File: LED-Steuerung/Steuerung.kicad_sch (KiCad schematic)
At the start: 45 parts, among them J1 DNP, J10 Barrel_Jack_Switch, J2 Conn_02x03_Odd_Even, J3 DNP, J4 Conn_01x01_Female, J5 Conn_01x01_Female, J6 Conn_01x01_Female, J7 Conn_01x01_Female, J8 Conn_01x01_Female, J9 Conn_01x01_Female, SW1 SW_Push, U1 STM32WB5MMG, U2 L7983, U3 INA186A3IDDF

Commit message: wip
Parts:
- added R11: 10k, Resistor_SMD:R_0603_1608Metric, symbol Device:R
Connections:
- net GND: now also R11.1; no longer U1.32 (VDDUSB)
- new net: R11.2, U1.32 (VDDUSB)
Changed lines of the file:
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@@
-    (stroke (width 0) (type default) (color 0 0 0 0))
-  )
-  (wire (pts (xy 71.12 66.04) (xy 71.12 68.58))
     (stroke (width 0) (type default) (color 0 0 0 0))
   )
@@
     (pin "1")
   )
-  (symbol (lib_id "power:GND") (at 71.12 66.04 180) (unit 1)
-    (in_bom yes) (on_board yes)
-    (property "Reference" "#PWR013" (id 0) (at 71.12 59.69 0)
-      (effects (font (size 1.27 1.27)) hide)
-    )
-    (property "Value" "GND" (id 1) (at 71.12 62.23 90)
-      (effects (font (size 1.27 1.27)) (justify right))
-    )
-    (property "Footprint" "" (id 2) (at 71.12 66.04 0)
-      (effects (font (size 1.27 1.27)) hide)
-    )
-    (property "Datasheet" "" (id 3) (at 71.12 66.04 0)
+  (symbol (lib_id "power:GND") (at 71.12 60.96 180) (unit 1)
+    (in_bom yes) (on_board yes)
+    (property "Reference" "#PWR013" (id 0) (at 71.12 54.61 0)
+      (effects (font (size 1.27 1.27)) hide)
+    )
+    (property "Value" "GND" (id 1) (at 71.12 57.15 90)
+      (effects (font (size 1.27 1.27)) (justify right))
+    )
+    (property "Footprint" "" (id 2) (at 71.12 60.96 0)
+      (effects (font (size 1.27 1.27)) hide)
+    )
+    (property "Datasheet" "" (id 3) (at 71.12 60.96 0)
       (effects (font (size 1.27 1.27)) hide)
     )
@@
     )
     (pin "1")
+  )
+  (symbol (lib_id "Device:R") (at 71.12 64.77 0) (unit 1)
+    (in_bom yes) (on_board yes)
+    (property "Reference" "R11" (id 0) (at 68.58 63.5 90)
+      (effects (font (size 1.27 1.27)) (justify right))
+    )
+    (property "Value" "10k" (id 1) (at 71.12 63.5 90)
+      (effects (font (size 1.27 1.27)) (justify right))
+    )
+    (property "Footprint" "Resistor_SMD:R_0603_1608Metric" (id 2) (at 69.342 64.77 90)
+      (effects (font (size 1.27 1.27)) hide)
+    )
+    (property "Datasheet" "~" (id 3) (at 71.12 64.77 0)
+      (effects (font (size 1.27 1.27)) hide)
+    )
+    (pin "1")
+    (pin "2")
   )
   (symbol (lib_id "power:+3.3V") (at 218.44 129.54 90) (unit 1)
@@
       (reference "R10") (unit 1) (value "1k5") (footprint "Resistor_SMD:R_0603_1608Metric")
     )
+    (path "/b412fb8f-9907-4294-9e36-0449a1743a06"
+      (reference "R11") (unit 1) (value "10k") (footprint "Resistor_SMD:R_0603_1608Metric")
+    )
     (path "/40f919cd-156f-42ae-a4b5-0e1a984d9708"

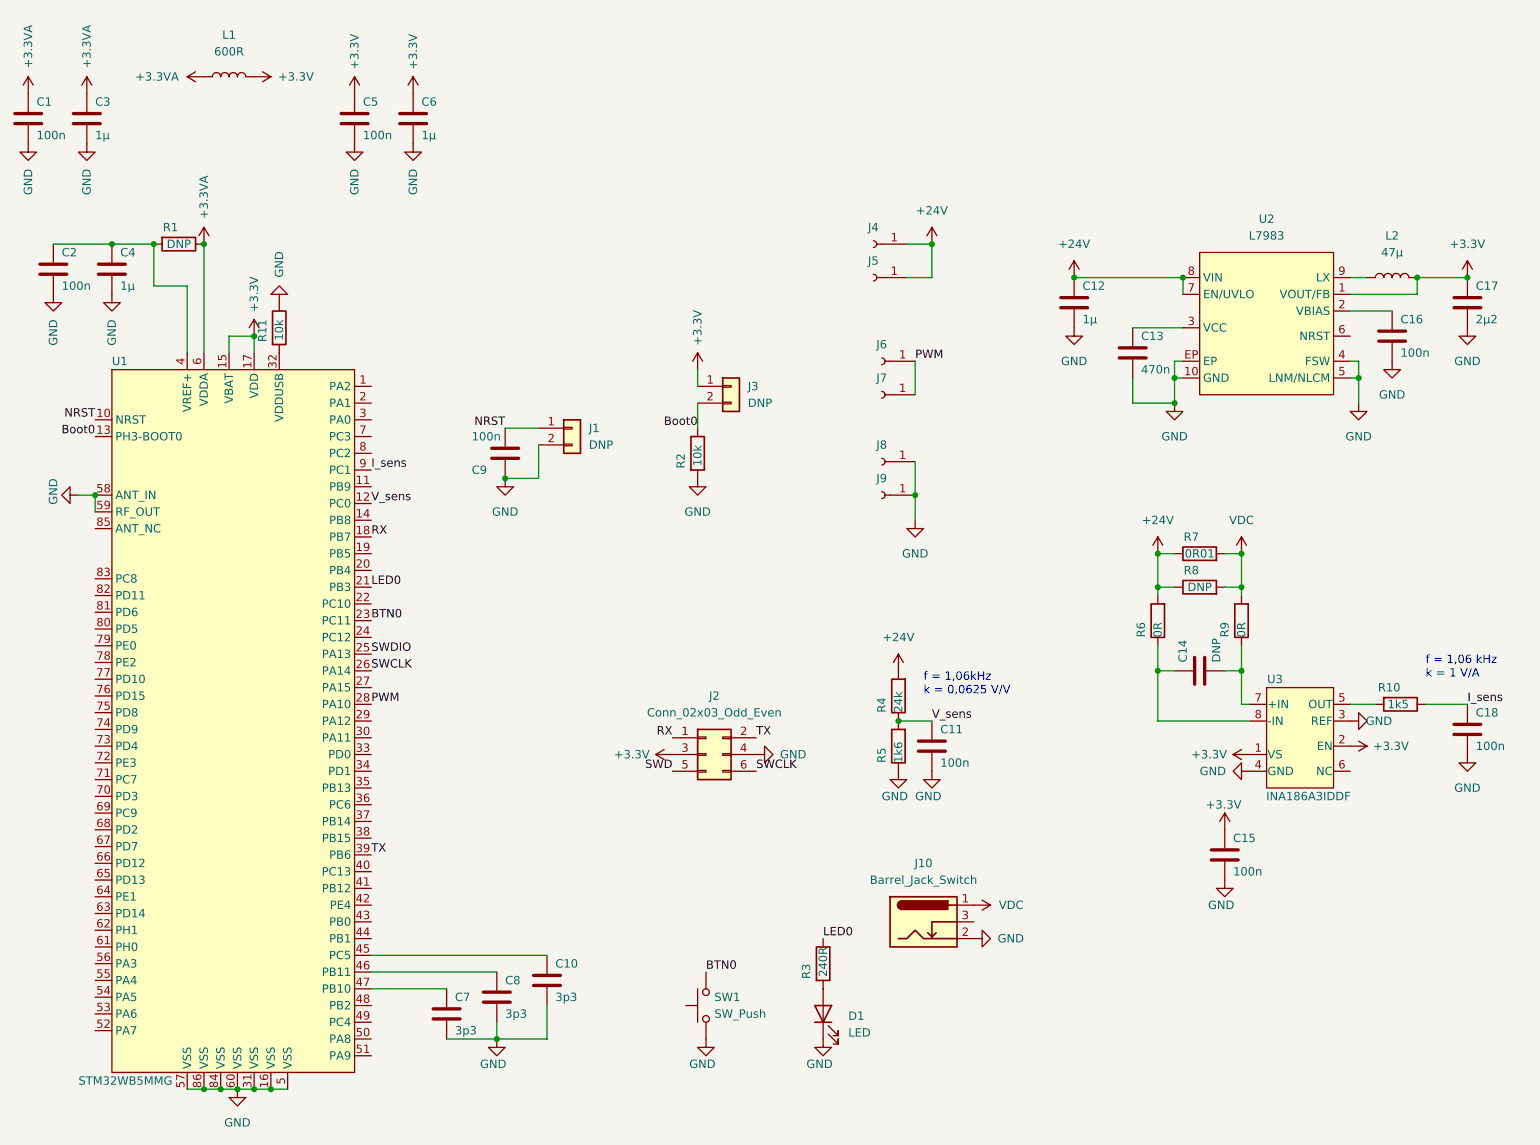
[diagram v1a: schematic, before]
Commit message: routed zigbee control
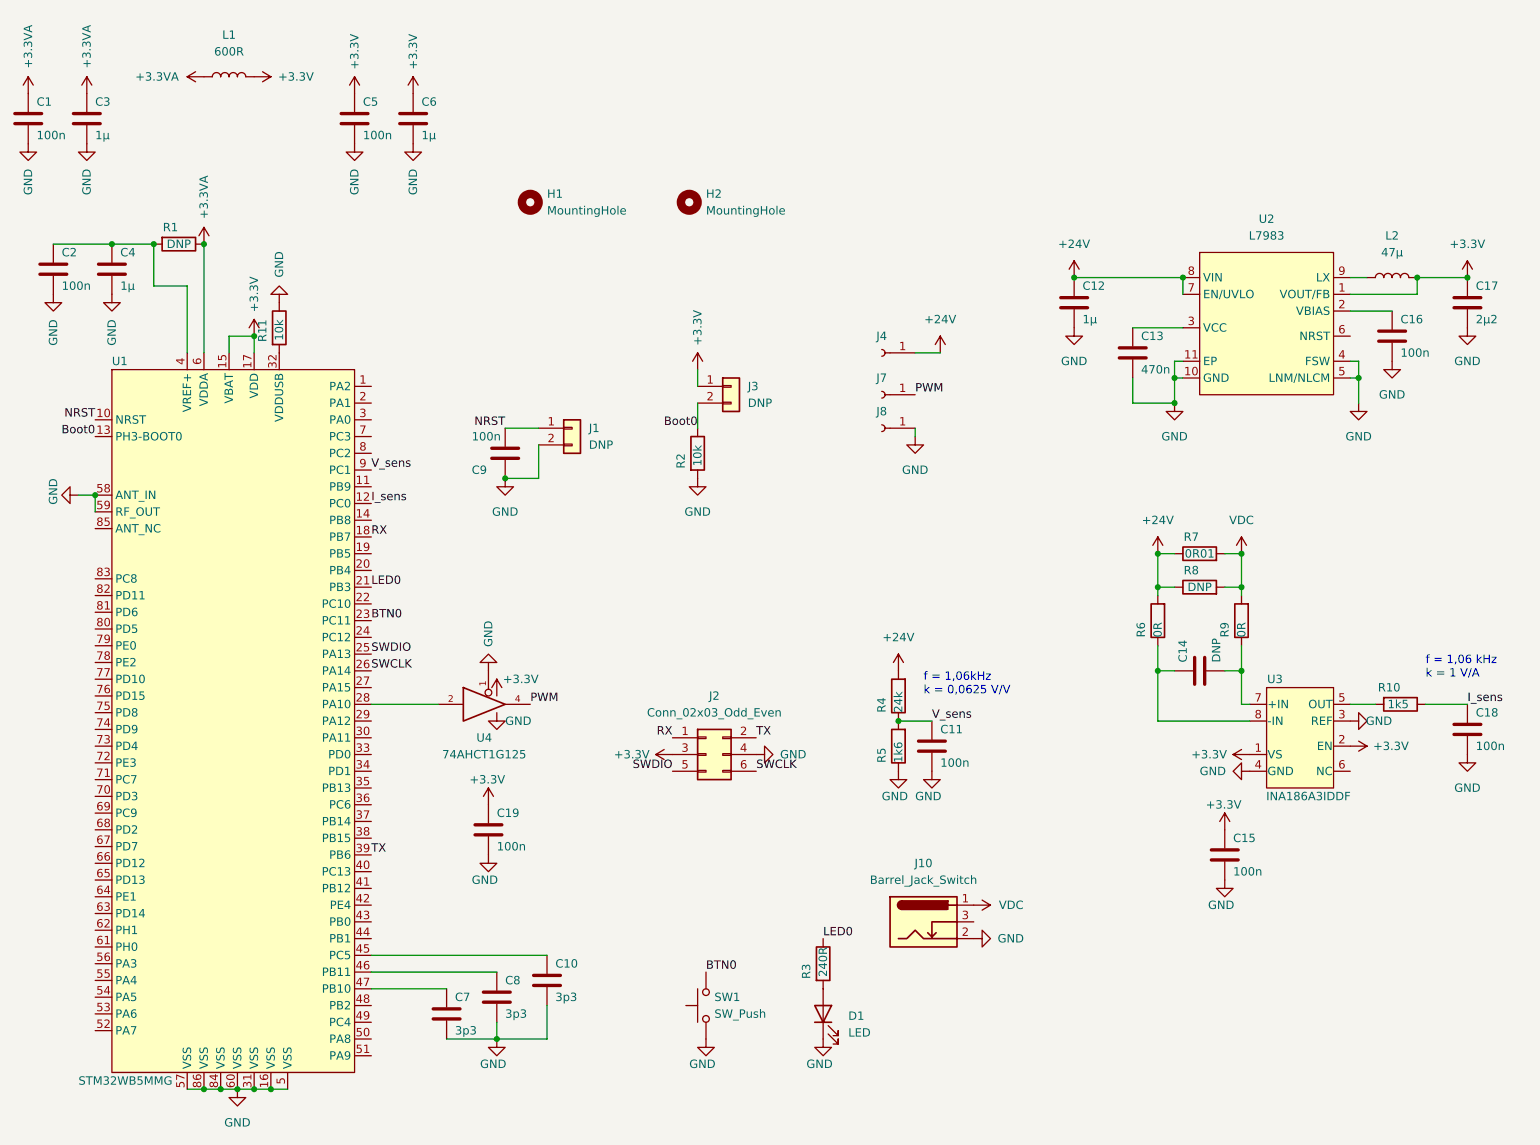
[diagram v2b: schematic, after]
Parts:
- removed J5, J6, J9: Conn_01x01_Female, Bergi:Solderpad_1x2, symbol Connector:Conn_01x01_Female
- added C19: 100n, Capacitor_SMD:C_0603_1608Metric, symbol Device:C
- added H1, H2: MountingHole, MountingHole:MountingHole_3.2mm_M3, symbol Mechanical:MountingHole
- added U4: 74AHCT1G125, Package_TO_SOT_SMD:SOT-353_SC-70-5, symbol 74xGxx:74AHCT1G125
- C1, C10, C2, C3, C5, C6, C7, C8: footprint Capacitor_SMD:C_0603_1608Metric -> Capacitor_SMD:C_0402_1005Metric
- C4: footprint Capacitor_SMD:C_0805_2012Metric -> Capacitor_SMD:C_0402_1005Metric
- L1: footprint Inductor_SMD:L_0603_1608Metric -> Inductor_SMD:L_0402_1005Metric
- R1: footprint Resistor_SMD:R_0603_1608Metric -> Capacitor_SMD:C_0402_1005Metric
- R11: footprint Resistor_SMD:R_0603_1608Metric -> Resistor_SMD:R_0402_1005Metric
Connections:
- net SWD is gone; now on net SWDIO: J2.5 (Pin_5)
- net +3.3V: now also C19.1, U4.5 (VCC)
- net GND: now also U2.11 (EP), C19.2, U4.1, U4.3 (GND); no longer U2.EP
- net I_sens: now also U1.12 (PC0); no longer U1.9 (PC1)
- net PWM: now also U4.4; no longer U1.28 (PA10)
- net V_sens: now also U1.9 (PC1); no longer U1.12 (PC0)
- new net: U1.28 (PA10), U4.2
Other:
- moved on the sheet: J4, J8
